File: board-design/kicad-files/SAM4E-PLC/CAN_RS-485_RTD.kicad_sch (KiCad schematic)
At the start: 65 parts, among them U10 MAX31865xAP, U6 SN65HVD230DR, U7 SN65HVD230DR, U8 MAX31865xAP, U9 MAX3485ESA+T

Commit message: [UPDATE]
First draft of SAM4E-PLC schematic completed.

Signed-off-by: Nicolae-Andrei Vasile <vasilenicolaeandrei@gmail.com>
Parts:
- removed U6, U7: SN65HVD230DR, digikey-footprints:SOIC-8_W3.9mm, symbol dk_Interface-Drivers-Receivers-Transceivers:SN65HVD230DR
- added U6, U7: SN65HVD234, Package_SO:SOIC-8_3.9x4.9mm_P1.27mm, symbol Interface_CAN_LIN:SN65HVD234
- JP3, JP4: footprint (none) -> Jumper:SolderJumper-2_P1.3mm_Open_Pad1.0x1.5mm
- R51: renamed from R44; footprint (none) -> Resistor_SMD:R_0603_1608Metric
- R52: renamed from R45; footprint (none) -> Resistor_SMD:R_0603_1608Metric
- renumbered C35 to C58, C36 to C59, C37 to C60, C38 to C61, C39 to C62, C40 to C63, C41 to C64, C42 to C65, C43 to C66, C44 to C67, C45 to C68, C46 to C69, C47 to C70, C48 to C71, C49 to C72, C50 to C73, C51 to C74, C52 to C75, C53 to C76, C54 to C77, C55 to C78, D4 to D3, R32 to R39, R33 to R40, R34 to R41, R35 to R42, R36 to R43, R37 to R44, R38 to R45, R39 to R46, R40 to R47, R41 to R48, R42 to R49, R43 to R50, R46 to R53, R47 to R54, R48 to R55, R49 to R56, R50 to R57, R51 to R58, R52 to R59, R53 to R60, R54 to R61, R55 to R62
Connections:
- net GND: now also U6.2 (GND), U7.2 (GND)
- net at C60.1, C62.1, L?.2: now also U6.3 (VCC)
- net at R44.2: now also U7.4 (R)
- net at R43.2, R50.1: now also U7.1 (D)
- net at R39.2, R49.1: now also U6.1 (D)
- net at R45.2, R48.2: now also U7.5 (EN)
- net at R40.2: now also U6.4 (R)
- net at R41.2, R47.2: now also U6.5 (EN)
- net at R42.2: now also U6.8 (Rs)
- net at C61.1, C63.1, L?.2: now also U7.3 (VCC)
- net at R46.2: now also U7.8 (Rs)
- net CAN0_H renamed MCV_CAN0_H
- net MCV_CAN0_H: now also U6.7 (CANH)
- net CAN0_L renamed MCV_CAN0_L
- net MCV_CAN0_L: now also U6.6 (CANL)
- net CAN1_H renamed MCV_CAN1_H
- net MCV_CAN1_H: now also U7.7 (CANH)
- net CAN1_L renamed MCV_CAN1_L
- net MCV_CAN1_L: now also U7.6 (CANL)
- net RS_A renamed MCV_RS_A
- net RS_B renamed MCV_RS_B
- net RTD0_FORCE+ renamed MCV_RTD0_FORCE+
- net RTD0_FORCE- renamed MCV_RTD0_FORCE-
- net RTD0_RTDIN+ renamed MCV_RTD0_RTDIN+
- net RTD0_RTDIN- renamed MCV_RTD0_RTDIN-
- net RTD1_FORCE+ renamed MCV_RTD1_FORCE+
- net RTD1_FORCE- renamed MCV_RTD1_FORCE-
- net RTD1_RTDIN+ renamed MCV_RTD1_RTDIN+
- net RTD1_RTDIN- renamed MCV_RTD1_RTDIN-

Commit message: [UPDATE]
Work in progress.

Signed-off-by: Nicolae-Andrei Vasile <vasilenicolaeandrei@gmail.com>
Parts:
- renumbered D3 to D4
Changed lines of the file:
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@@
   (symbol (lib_id "Device:D_TVS_Dual_AAC") (at 359.41 232.41 0) (unit 1)
     (in_bom yes) (on_board yes) (dnp no) (fields_autoplaced)
-    (property "Reference" "D3" (at 359.41 226.06 0)
+    (property "Reference" "D4" (at 359.41 226.06 0)
       (effects (font (size 1.27 1.27)))
     )
@@
       (project "SAM4E-PLC"
         (path "/93076d8a-73da-4f5d-b7f2-28678f1db77d/32910dfe-b730-4651-8391-975b8cdac59d"
-          (reference "D3") (unit 1)
+          (reference "D4") (unit 1)
         )
       )

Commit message: [UPDATE]
Work in progress.

Signed-off-by: Nicolae-Andrei Vasile <vasilenicolaeandrei@gmail.com>
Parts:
- renumbered C58 to C59, C59 to C60, C60 to C61, C61 to C62, C62 to C63, C63 to C64, C64 to C65, C65 to C66, C66 to C67, C67 to C68, C68 to C69, C69 to C70, C70 to C71, C71 to C72, C72 to C73, C73 to C74, C74 to C75, C75 to C76, C76 to C77, C77 to C78, C78 to C79

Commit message: [UPDATE]
Work in progress.

Signed-off-by: Nicolae-Andrei Vasile <vasilenicolaeandrei@gmail.com>
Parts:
- renumbered C59 to C61, C60 to C62, C61 to C63, C62 to C64, C63 to C65, C64 to C66, C65 to C67, C66 to C68, C67 to C69, C68 to C70, C69 to C71, C70 to C72, C71 to C73, C72 to C74, C73 to C75, C74 to C76, C75 to C77, C76 to C78, C77 to C79, C78 to C80, C79 to C81, D4 to D5
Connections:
- net CAN0_D: now also R44.1; no longer R40.1
- net CAN0_EN: now also R45.1; no longer R41.1
- net CAN0_R: now also R46.1; no longer R42.1
- net CAN0_RS: now also R43.1; no longer R39.1
- net CAN1_D: now also R40.1; no longer R44.1
- net CAN1_EN: now also R41.1; no longer R45.1
- net CAN1_R: now also R42.1; no longer R46.1
- net CAN1_RS: now also R39.1; no longer R43.1
- net MCV_CAN0_H: now also JP4.2 (B), U7.7 (CANH); no longer JP3.2 (B), U6.7 (CANH)
- net MCV_CAN0_L: now also R52.1, U7.6 (CANL); no longer R51.1, U6.6 (CANL)
- net MCV_CAN1_H: now also JP3.2 (B), U6.7 (CANH); no longer JP4.2 (B), U7.7 (CANH)
- net MCV_CAN1_L: now also R51.1, U6.6 (CANL); no longer R52.1, U7.6 (CANL)

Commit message: [UPDATE]
Work in progress.

Signed-off-by: Nicolae-Andrei Vasile <vasilenicolaeandrei@gmail.com>
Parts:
- renumbered C61 to C37, C62 to C38, C63 to C39, C64 to C40, C65 to C41, C66 to C42, C67 to C43, C68 to C44, C69 to C45, C70 to C46, C71 to C47, C72 to C48, C73 to C49, C74 to C50, C75 to C51, C76 to C52, C77 to C53, C78 to C54, C79 to C55, C80 to C56, C81 to C57, D5 to D3, JP9 to JP10, JP10 to JP11, JP11 to JP12, JP3 to JP4, JP4 to JP5, JP5 to JP6, JP6 to JP7, JP7 to JP8, JP8 to JP9, R39 to R14, R40 to R15, R41 to R16, R42 to R17, R43 to R18, R44 to R19, R45 to R20, R46 to R21, R47 to R22, R48 to R23, R49 to R24, R50 to R25, R51 to R26, R52 to R27, R53 to R28, R54 to R29, R55 to R30, R56 to R31, R57 to R32, R58 to R33, R59 to R34, R60 to R35, R61 to R36, R62 to R37, U6 to U3, U7 to U4, U8 to U5, U9 to U6, U10 to U7

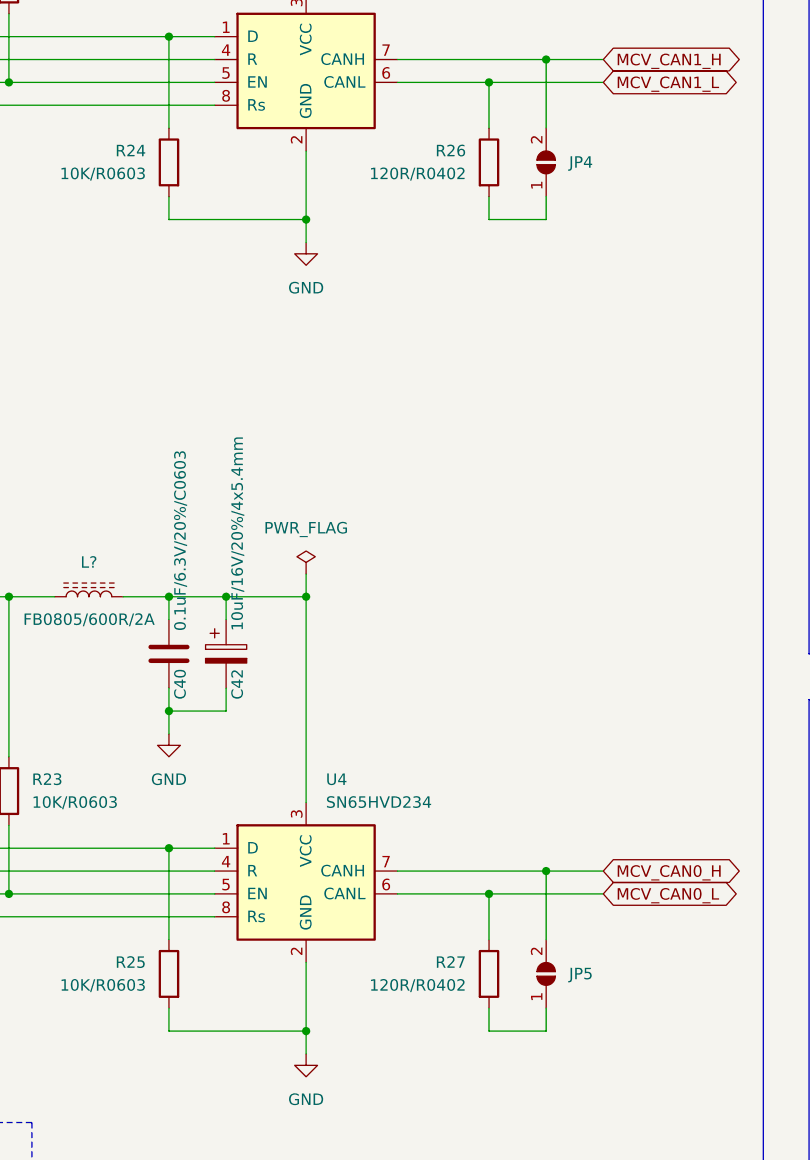
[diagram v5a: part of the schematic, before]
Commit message: [UPDATE]
Completed SAM4E-PLC board design.

Signed-off-by: Nicolae-Andrei Vasile <vasilenicolaeandrei@gmail.com>
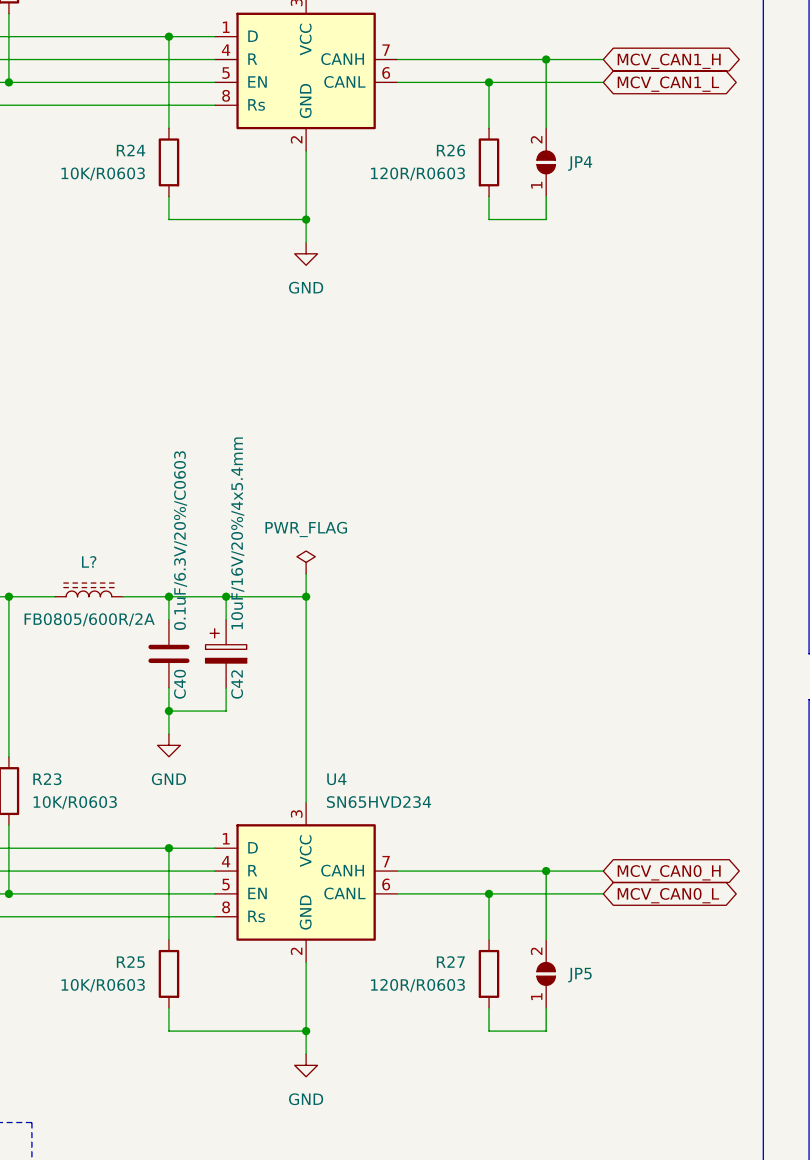
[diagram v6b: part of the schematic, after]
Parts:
- R26, R27: value 120R/R0402 -> 120R/R0603
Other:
- title: CAN, RS-422/485, RTD -> SAM4E

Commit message: [Final report]
Added 3D models.

Signed-off-by: Nicolae-Andrei Vasile <vasilenicolaeandrei@gmail.com>
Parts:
- gave numbers to parts that had none: 5
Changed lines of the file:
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@@
   (symbol (lib_id "Device:L_Ferrite") (at 77.47 55.88 90) (unit 1)
     (in_bom yes) (on_board yes) (dnp no)
-    (property "Reference" "L?" (at 77.47 52.07 90)
+    (property "Reference" "L3" (at 77.47 52.07 90)
       (effects (font (size 1.27 1.27)))
     )
@@
     (instances
       (project "SAM4E-PLC"
-        (path "/93076d8a-73da-4f5d-b7f2-28678f1db77d/aee81a7b-cba1-4b89-a883-459d3f783e91"
-          (reference "L?") (unit 1)
-        )
-        (path "/93076d8a-73da-4f5d-b7f2-28678f1db77d/f76e13f7-6a24-4ea6-98c5-a4d0bd3b3ced"
-          (reference "L?") (unit 1)
-        )
         (path "/93076d8a-73da-4f5d-b7f2-28678f1db77d/32910dfe-b730-4651-8391-975b8cdac59d"
           (reference "L3") (unit 1)
@@
   (symbol (lib_id "Device:L_Ferrite") (at 289.56 72.39 90) (unit 1)
     (in_bom yes) (on_board yes) (dnp no)
-    (property "Reference" "L?" (at 289.56 68.58 90)
+    (property "Reference" "L7" (at 289.56 68.58 90)
       (effects (font (size 1.27 1.27)))
     )
@@
     (instances
       (project "SAM4E-PLC"
-        (path "/93076d8a-73da-4f5d-b7f2-28678f1db77d/aee81a7b-cba1-4b89-a883-459d3f783e91"
-          (reference "L?") (unit 1)
-        )
-        (path "/93076d8a-73da-4f5d-b7f2-28678f1db77d/f76e13f7-6a24-4ea6-98c5-a4d0bd3b3ced"
-          (reference "L?") (unit 1)
-        )
         (path "/93076d8a-73da-4f5d-b7f2-28678f1db77d/32910dfe-b730-4651-8391-975b8cdac59d"
           (reference "L7") (unit 1)
@@
   (symbol (lib_id "Device:L_Ferrite") (at 77.47 146.05 90) (unit 1)
     (in_bom yes) (on_board yes) (dnp no)
-    (property "Reference" "L?" (at 77.47 142.24 90)
+    (property "Reference" "L4" (at 77.47 142.24 90)
       (effects (font (size 1.27 1.27)))
     )
@@
     (instances
       (project "SAM4E-PLC"
-        (path "/93076d8a-73da-4f5d-b7f2-28678f1db77d/aee81a7b-cba1-4b89-a883-459d3f783e91"
-          (reference "L?") (unit 1)
-        )
-        (path "/93076d8a-73da-4f5d-b7f2-28678f1db77d/f76e13f7-6a24-4ea6-98c5-a4d0bd3b3ced"
-          (reference "L?") (unit 1)
-        )
         (path "/93076d8a-73da-4f5d-b7f2-28678f1db77d/32910dfe-b730-4651-8391-975b8cdac59d"
           (reference "L4") (unit 1)
@@
   (symbol (lib_id "Device:L_Ferrite") (at 172.72 72.39 90) (unit 1)
     (in_bom yes) (on_board yes) (dnp no)
-    (property "Reference" "L?" (at 172.72 68.58 90)
+    (property "Reference" "L5" (at 172.72 68.58 90)
       (effects (font (size 1.27 1.27)))
     )
@@
     (instances
       (project "SAM4E-PLC"
-        (path "/93076d8a-73da-4f5d-b7f2-28678f1db77d/aee81a7b-cba1-4b89-a883-459d3f783e91"
-          (reference "L?") (unit 1)
-        )
-        (path "/93076d8a-73da-4f5d-b7f2-28678f1db77d/f76e13f7-6a24-4ea6-98c5-a4d0bd3b3ced"
-          (reference "L?") (unit 1)
-        )
         (path "/93076d8a-73da-4f5d-b7f2-28678f1db77d/32910dfe-b730-4651-8391-975b8cdac59d"
           (reference "L5") (unit 1)
@@
   (symbol (lib_id "Device:L_Ferrite") (at 271.78 177.8 90) (unit 1)
     (in_bom yes) (on_board yes) (dnp no)
-    (property "Reference" "L?" (at 271.78 173.99 90)
+    (property "Reference" "L6" (at 271.78 173.99 90)
       (effects (font (size 1.27 1.27)))
     )
@@
     (instances
       (project "SAM4E-PLC"
-        (path "/93076d8a-73da-4f5d-b7f2-28678f1db77d/aee81a7b-cba1-4b89-a883-459d3f783e91"
-          (reference "L?") (unit 1)
-        )
-        (path "/93076d8a-73da-4f5d-b7f2-28678f1db77d/f76e13f7-6a24-4ea6-98c5-a4d0bd3b3ced"
-          (reference "L?") (unit 1)
-        )
         (path "/93076d8a-73da-4f5d-b7f2-28678f1db77d/32910dfe-b730-4651-8391-975b8cdac59d"
           (reference "L6") (unit 1)
